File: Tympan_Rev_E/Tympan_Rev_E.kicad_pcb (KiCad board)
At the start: 4 copper layers, 38 x 74 mm, 92 parts, among them IC1 BC127, J1 SJ-3523-SMT-TR, J2 SJ-3524-SMT-TR-PI, J4 Conn_01x03, J5 Conn_01x24, J6 Conn_01x24, P1 CONN_01X06, P2 CONN_01X06, P3 CONN_01X06, P4 CONN_01X06, P6 CONN_01X01, P7 CONN_01X01, P8 CONN_01X01, SW1 CL-SB-22A, SW2 TACT_SWITCH, U1 MCP73831, U2 TLV320AIC3206IRSBT, U3 74LVC1G66, U4 LP5907MFX-1.8, U5 Teensy4.1, U6 LC709203

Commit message: fixes to silk and delete unused tracks
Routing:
- net /L: track 21.4 -> 9.26 mm
- net /R: track 28.2 -> 21.5 mm
- net /IN2_R: track 33.0 -> 31.1 mm

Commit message: moved ICP Shield header
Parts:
- removed J4: Conn_01x03, Pin_Headers:Pin_Header_Straight_1x03_Pitch2.00mm
- added J3: Conn_01x04, Pin_Headers:Pin_Header_Straight_1x04_Pitch2.00mm, F.Cu at (135.6, 126.7)
- moved BT1 0.45 mm to (144.4, 126.7)
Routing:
- net /SW_BATT: track 15.1 -> 20.7 mm
- net +BATT: track 52.6 -> 55.8 mm
- net /V_BAT: track 55.9 -> 57.9 mm

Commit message: added 2 more breakouts
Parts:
- J3: value Conn_01x04 -> Conn_01x06; footprint Pin_Headers:Pin_Header_Straight_1x04_Pitch2.00mm -> Pin_Headers:Pin_Header_Straight_1x06_Pitch2.00mm
- moved J3 4.05 mm to (135.4, 130.8)
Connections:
- J3 pad 1: /V_BAT -> /35_TX8
- J3 pad 2: /SW_BATT -> /34_RX8
- J3 pad 3: +BATT -> /V_BAT
- J3 pad 4: GND -> /SW_BATT
- U5 pad 26: Net-(U5-Pad26) -> /34_RX8
- U5 pad 27: Net-(U5-Pad27) -> /35_TX8
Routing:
- net /35_TX8: track 0.00 -> 79.6 mm, vias 0 -> 3
- net /34_RX8: track 0.00 -> 76.0 mm, vias 0 -> 3
- net /WCLK: track 49.0 -> 47.4 mm
- net /BT_PIO5: track 10.4 -> 9.10 mm
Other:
- board text added: "GND +BATT SW_BAT 34 35"

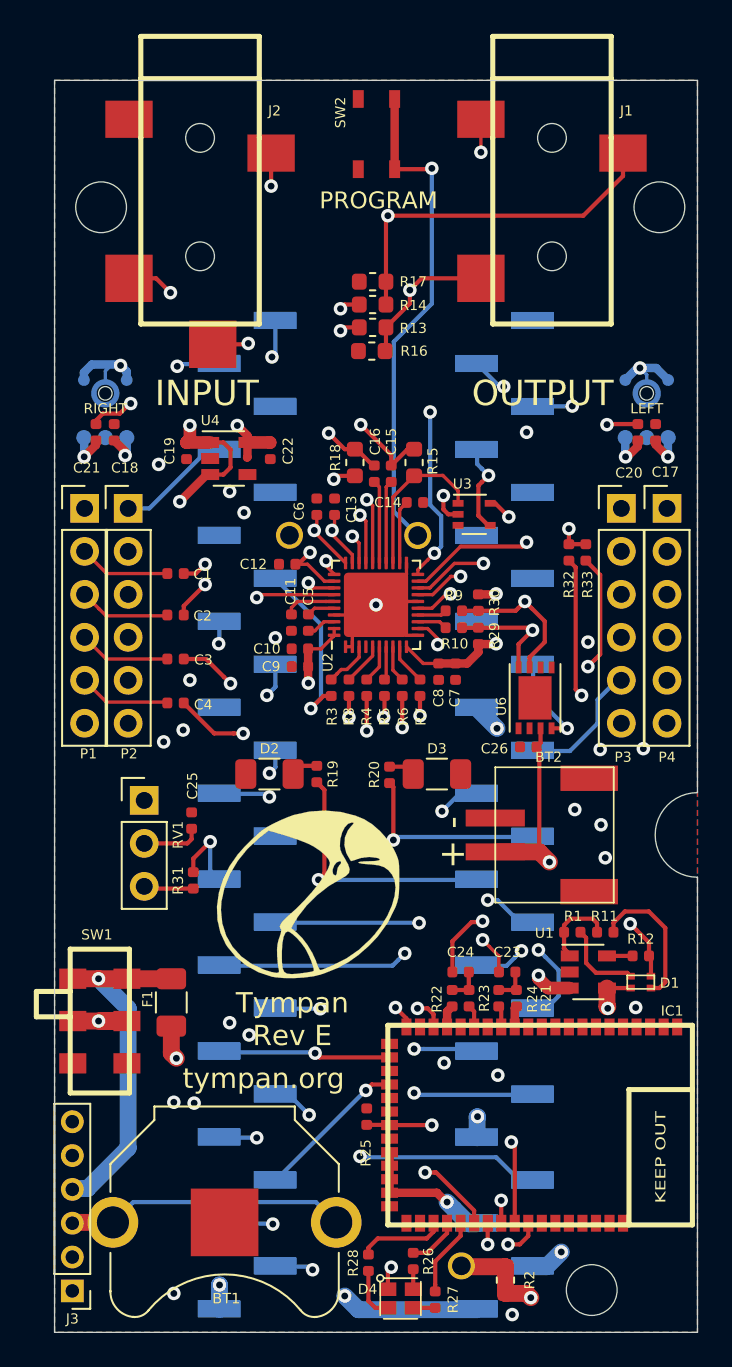
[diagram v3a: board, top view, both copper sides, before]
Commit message: Added through hole prog button and Qwiic connector
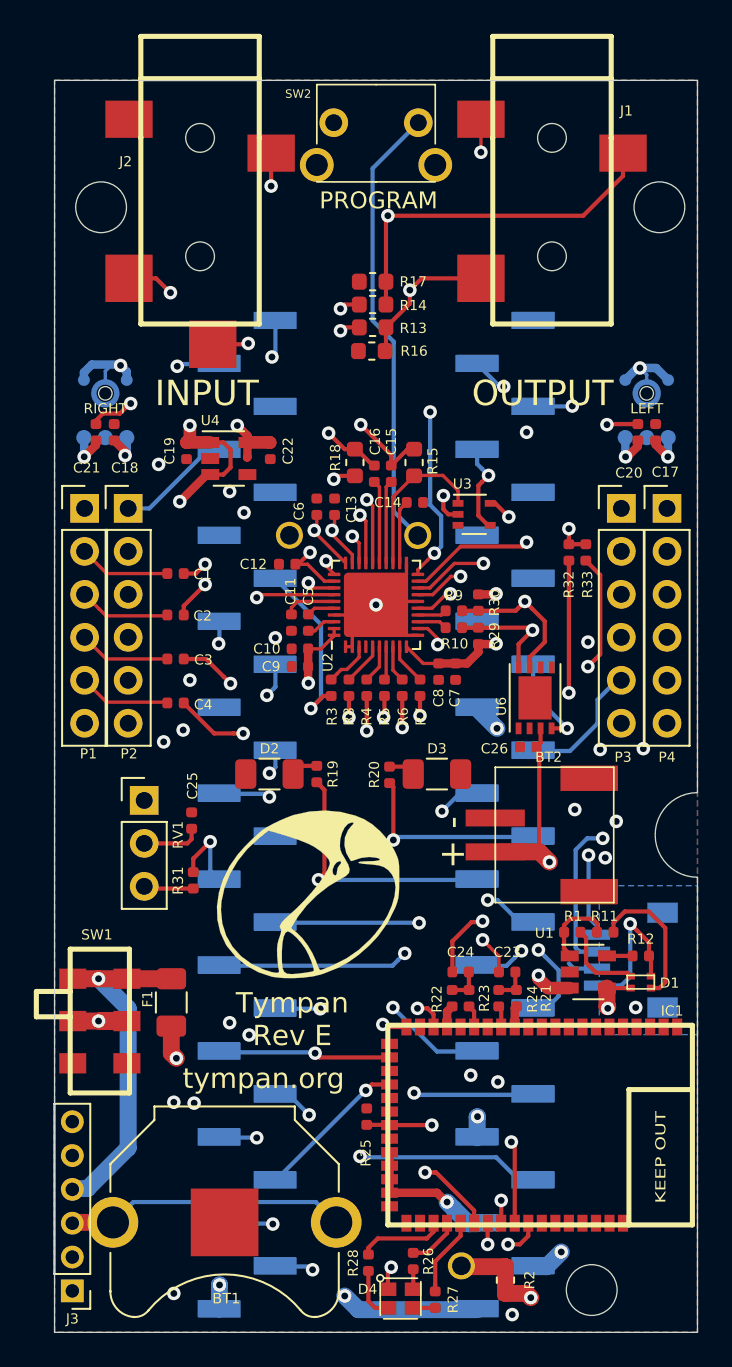
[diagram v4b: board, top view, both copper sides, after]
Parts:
- added J4: Qwiik Connector, Connectors_JST:JST_SH_SM04B-SRSS-TB_04x1.00mm_Angled, B.Cu at (168.4, 111.2)
- SW2: value TACT_SWITCH -> SW_Push; footprint Tympan:PTS810 -> Tympan:MJTP1117
- moved G*** 1.75 mm to (153.4, 68.7)
- moved SW2 0.45 mm to (153.4, 61.7), turned to 180 degrees
- moved J6 0.06 mm to (161.1, 102.6)
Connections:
- SW2 pad 2: /PROGRAM -> GND
- SW2 pad 3: GND -> (no net)
- SW2 pad 4: GND -> (no net)
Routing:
- net /SDA2: track 36.0 -> 55.5 mm, vias 2 -> 3
- net /SCL2: track 34.6 -> 49.3 mm, vias 2 -> 3
- net GND: track 71.1 -> 76.4 mm
- net /PROGRAM: track 29.6 -> 26.6 mm, vias 1 -> 0
- net +3V3: track 31.9 -> 33.7 mm
- net /34_RX8: track 76.0 -> 77.7 mm
- net /LOL: track 58.6 -> 57.6 mm
- net /WCLK: track 47.4 -> 46.7 mm
- net /35_TX8: track 79.6 -> 80.2 mm
- added copper zone on B.Cu, net GND

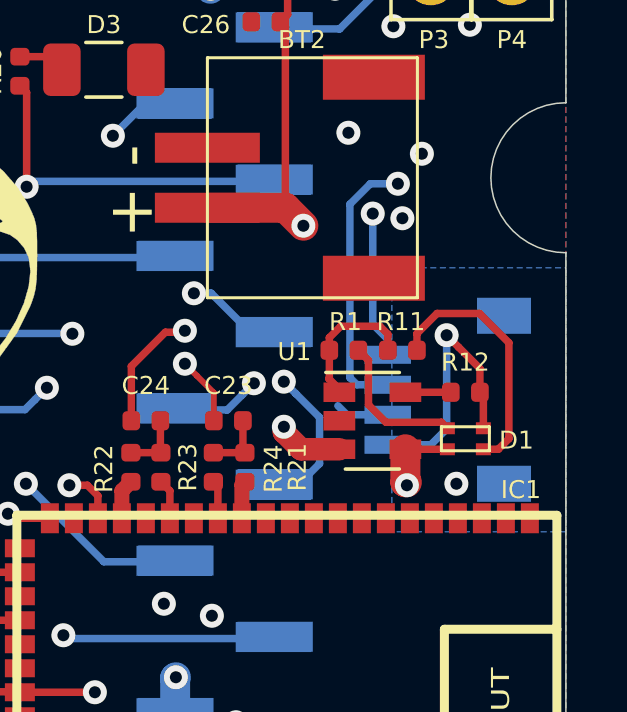
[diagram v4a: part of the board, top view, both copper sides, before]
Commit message: Verified Qwiic pin order
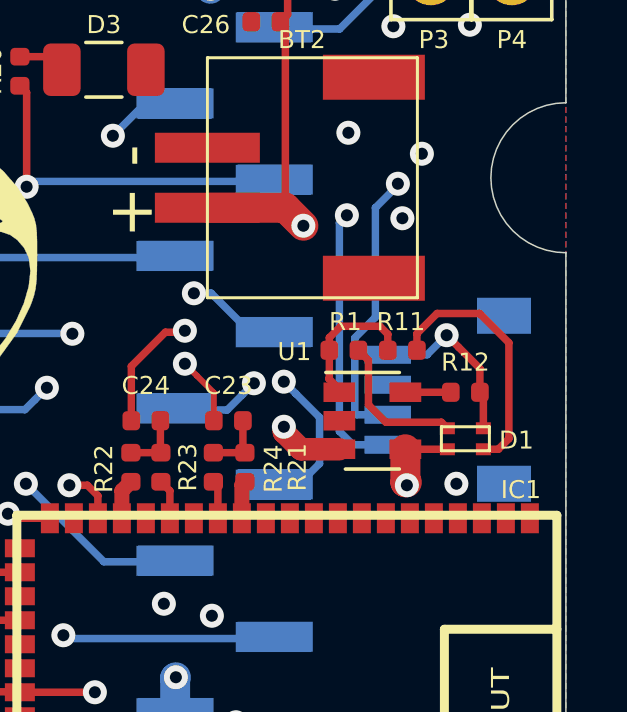
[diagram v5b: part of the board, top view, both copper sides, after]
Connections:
- J4 pad : GND -> (no net)
- J4 pad 1: /SCL2 -> GND
- J4 pad 2: /SDA2 -> +3V3
- J4 pad 3: +3V3 -> /SDA2
- J4 pad 4: GND -> /SCL2
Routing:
- net /SCL2: track 49.3 -> 53.9 mm
- net GND: track 76.4 -> 73.4 mm
- net +3V3: track 33.7 -> 31.9 mm
- removed copper zone on B.Cu, net GND

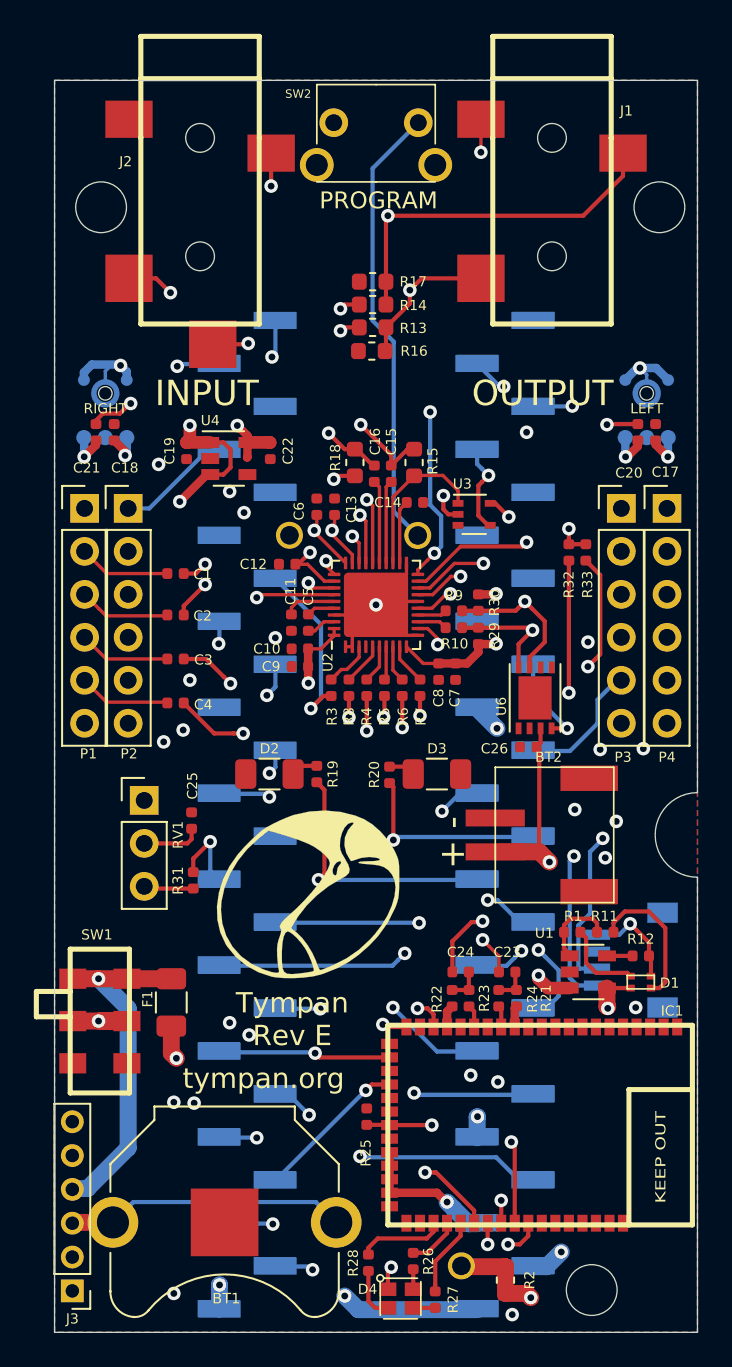
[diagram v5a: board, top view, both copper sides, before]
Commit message: Final Review
Adjust silk and some internal traces.
add net names to SMT headers for DFM and placement
publish up to date PDF
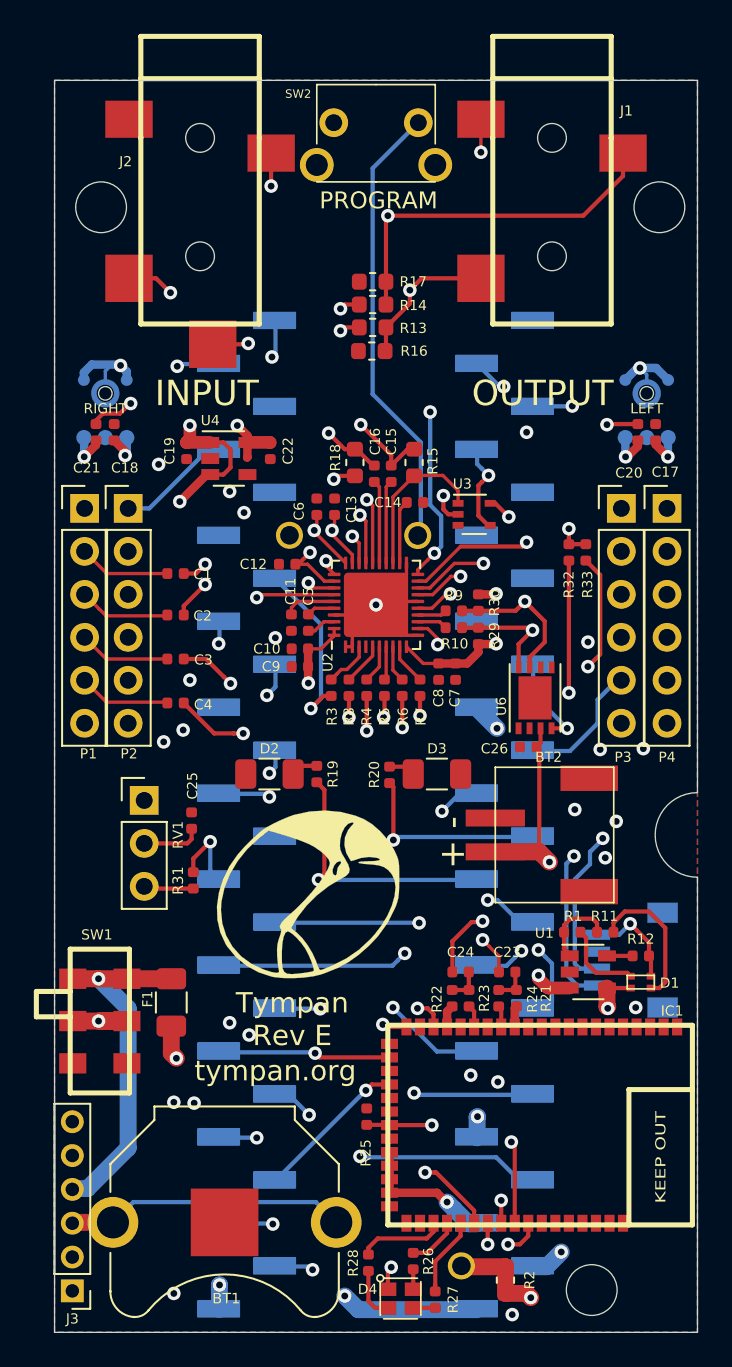
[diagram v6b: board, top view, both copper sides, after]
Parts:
- J5, J6: value Conn_01x24 -> SMT
- moved J6 0.05 mm to (161.0, 102.6)
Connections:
- J4 pad : (no net) -> +3V3
- J5 pad 1: Net-(J5-Pad1) -> GND
- J5 pad 10: Net-(J5-Pad10) -> /DOUT
- J5 pad 11: Net-(J5-Pad11) -> /BT_nRESET
- J5 pad 12: Net-(J5-Pad12) -> /SS
- J5 pad 13: Net-(J5-Pad13) -> /MOSI
- J5 pad 14: Net-(J5-Pad14) -> /MISO
- J5 pad 16: Net-(J5-Pad16) -> /SCL2
- J5 pad 17: Net-(J5-Pad17) -> /SDA2
- J5 pad 18: Net-(J5-Pad18) -> /nRESET
- J5 pad 2: Net-(J5-Pad2) -> /BT_TX
- J5 pad 21: Net-(J5-Pad21) -> /M_BIAS_1
- J5 pad 23: Net-(J5-Pad23) -> /nRESET_1
- J5 pad 24: Net-(J5-Pad24) -> /DIN_1
- J5 pad 3: Net-(J5-Pad3) -> /BT_RX
- J5 pad 4: Net-(J5-Pad4) -> /BT_PIO5
- J5 pad 5: Net-(J5-Pad5) -> /BT_CTS
- J5 pad 6: Net-(J5-Pad6) -> /BT_RTS
- J5 pad 7: Net-(J5-Pad7) -> /BT_PIO0
- J5 pad 8: Net-(J5-Pad8) -> /DOUT_1
- J5 pad 9: Net-(J5-Pad9) -> /DIN
- J6 pad 10: Net-(J6-Pad10) -> GND
- J6 pad 11: Net-(J6-Pad11) -> /SCK
- J6 pad 12: Net-(J6-Pad12) -> /VREGEN
- J6 pad 13: Net-(J6-Pad13) -> /LED_A
- J6 pad 14: Net-(J6-Pad14) -> /LED_R
- J6 pad 15: Net-(J6-Pad15) -> /POT
- J6 pad 16: Net-(J6-Pad16) -> /SDA
- J6 pad 17: Net-(J6-Pad17) -> /SCL
- J6 pad 18: Net-(J6-Pad18) -> /WCLK
- J6 pad 19: Net-(J6-Pad19) -> /BCLK
- J6 pad 2: Net-(J6-Pad2) -> /34_RX8
- J6 pad 20: Net-(J6-Pad20) -> GND
- J6 pad 21: Net-(J6-Pad21) -> /MCLK
- J6 pad 23: Net-(J6-Pad23) -> GND
- J6 pad 24: Net-(J6-Pad24) -> /VIN
- J6 pad 3: Net-(J6-Pad3) -> /35_TX8
- J6 pad 4: Net-(J6-Pad4) -> /M_BIAS
- J6 pad 9: Net-(J6-Pad9) -> /ALARMB
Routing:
- net /V_BAT: track 57.9 -> 60.3 mm
- net /HPR: track 23.5 -> 24.1 mm
- net /35_TX8: track 80.2 -> 79.7 mm

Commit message: Updated Silk
added version and note next to Quiic/Stemma connector
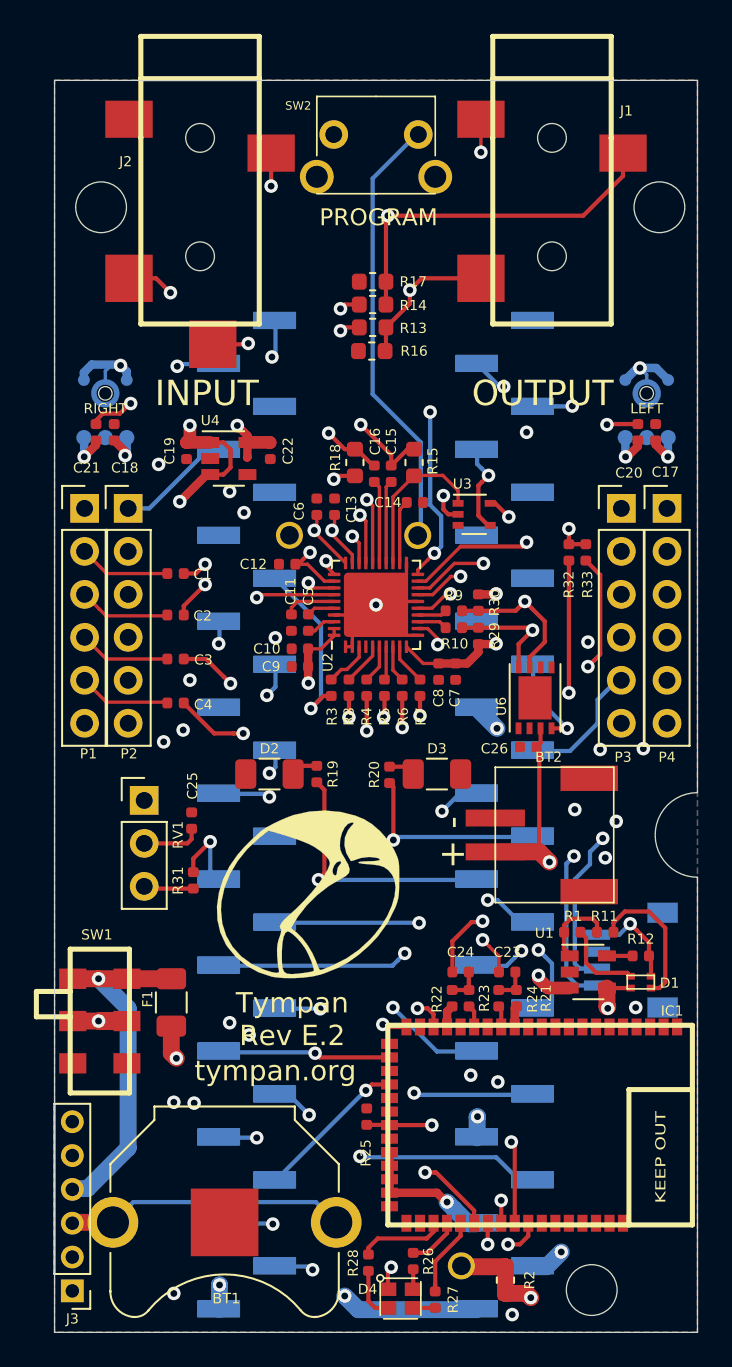
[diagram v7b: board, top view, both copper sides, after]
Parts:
- moved SW2 0.70 mm to (153.4, 62.4)
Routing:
- net /PROGRAM: track 26.8 -> 26.2 mm
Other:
- board text added: "Qwiic ———> Stemma"
- board text added: "Tympan Rev E.2"
- board text removed: "Tympan Rev E"
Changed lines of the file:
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@@
   (general
     (thickness 1.6)
-    (drawings 24)
+    (drawings 25)
     (tracks 960)
     (zones 0)
@@
   (page A4)
   (layers
-    (0 F.Cu mixed)
-    (1 In1.Cu mixed)
-    (2 In2.Cu mixed)
+    (0 F.Cu mixed hide)
+    (1 In1.Cu mixed hide)
+    (2 In2.Cu mixed hide)
     (31 B.Cu mixed)
     (32 B.Adhes user hide)
     (33 F.Adhes user hide)
     (34 B.Paste user)
-    (35 F.Paste user)
+    (35 F.Paste user hide)
     (36 B.SilkS user)
-    (37 F.SilkS user)
+    (37 F.SilkS user hide)
     (38 B.Mask user)
-    (39 F.Mask user)
+    (39 F.Mask user hide)
     (40 Dwgs.User user hide)
     (41 Cmts.User user hide)
@@
   (module teensy:Teensy41_SMT (layer B.Cu)
     (at 153.365 102.6 90)
-    (fp_text reference U5 (at 0 10.16 90) (layer B.SilkS)
+    (fp_text reference U5 (at 3 -2.665 180) (layer B.SilkS)
       (effects (font (size 1 1) (thickness 0.15)) (justify mirror))
     )
@@
   )
   (module Tympan:MJTP1117 (layer F.Cu)
-    (at 153.4 61.7 180)
+    (at 153.4 62.4 180)
     (fp_text reference SW2 (at 4.6 1.7) (layer F.SilkS)
       (effects (font (size 0.5 0.5) (thickness 0.125)))
@@
       (net 2 GND))
   )
+  (gr_text "Qwiic\n———>\nStemma" (at 166.9 107.9 90) (layer B.SilkS)
+    (effects (font (size 0.6 0.6) (thickness 0.125)) (justify right mirror))
+  )
   (gr_text "GND\n+BATT\nSW_BAT\n\n\n34\n35" (at 136.9 125.95) (layer B.SilkS)
     (effects (font (size 1 0.6) (thickness 0.125)) (justify right mirror))
@@
   (gr_line (start 155.15 60) (end 155.15 64.7) (layer Dwgs.User) (width 0.15))
   (gr_line (start 151.75 60) (end 155.15 60) (layer Dwgs.User) (width 0.15))
-  (gr_text PROGRAM (at 153.55 66.3) (layer F.SilkS)
+  (gr_text PROGRAM (at 153.55 67.3) (layer F.SilkS)
     (effects (font (size 1 1) (thickness 0.15)))
   )
@@
     (effects (font (size 1.2 1.2) (thickness 0.2)))
   )
-  (gr_text "Tympan\nRev E" (at 148.45 114.7) (layer F.SilkS)
+  (gr_text "Tympan\nRev E.2" (at 148.45 114.7) (layer F.SilkS)
     (effects (font (size 1.2 1.2) (thickness 0.2)))
   )
@@
   (segment (start 156.05 85.915) (end 155.865 86.1) (width 0.25) (layer B.Cu) (net 140))
   (segment (start 153.2 77.75) (end 156.05 80.6) (width 0.25) (layer B.Cu) (net 140))
-  (segment (start 153.2 64.4) (end 153.2 77.75) (width 0.25) (layer B.Cu) (net 140))
+  (segment (start 153.2 65) (end 153.2 77.75) (width 0.25) (layer B.Cu) (net 140))
+  (segment (start 155.9 62.3) (end 153.2 65) (width 0.25) (layer B.Cu) (net 140))
   (segment (start 156.05 80.6) (end 156.05 85.915) (width 0.25) (layer B.Cu) (net 140))
-  (segment (start 155.9 61.7) (end 153.2 64.4) (width 0.25) (layer B.Cu) (net 140))
   (segment (start 138.675 112.3) (end 137 112.3) (width 1) (layer F.Cu) (net 141))
   (segment (start 137 112.3) (end 135.475 112.3) (width 1) (layer F.Cu) (net 141))
